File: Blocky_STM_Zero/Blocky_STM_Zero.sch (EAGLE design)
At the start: 37 parts, among them IC3 MCP1703CB, J1 2P-2.0-90D-SMD, U1 MCP73831, U2 STM32L053R8T6, X5 8MHz(16pF)

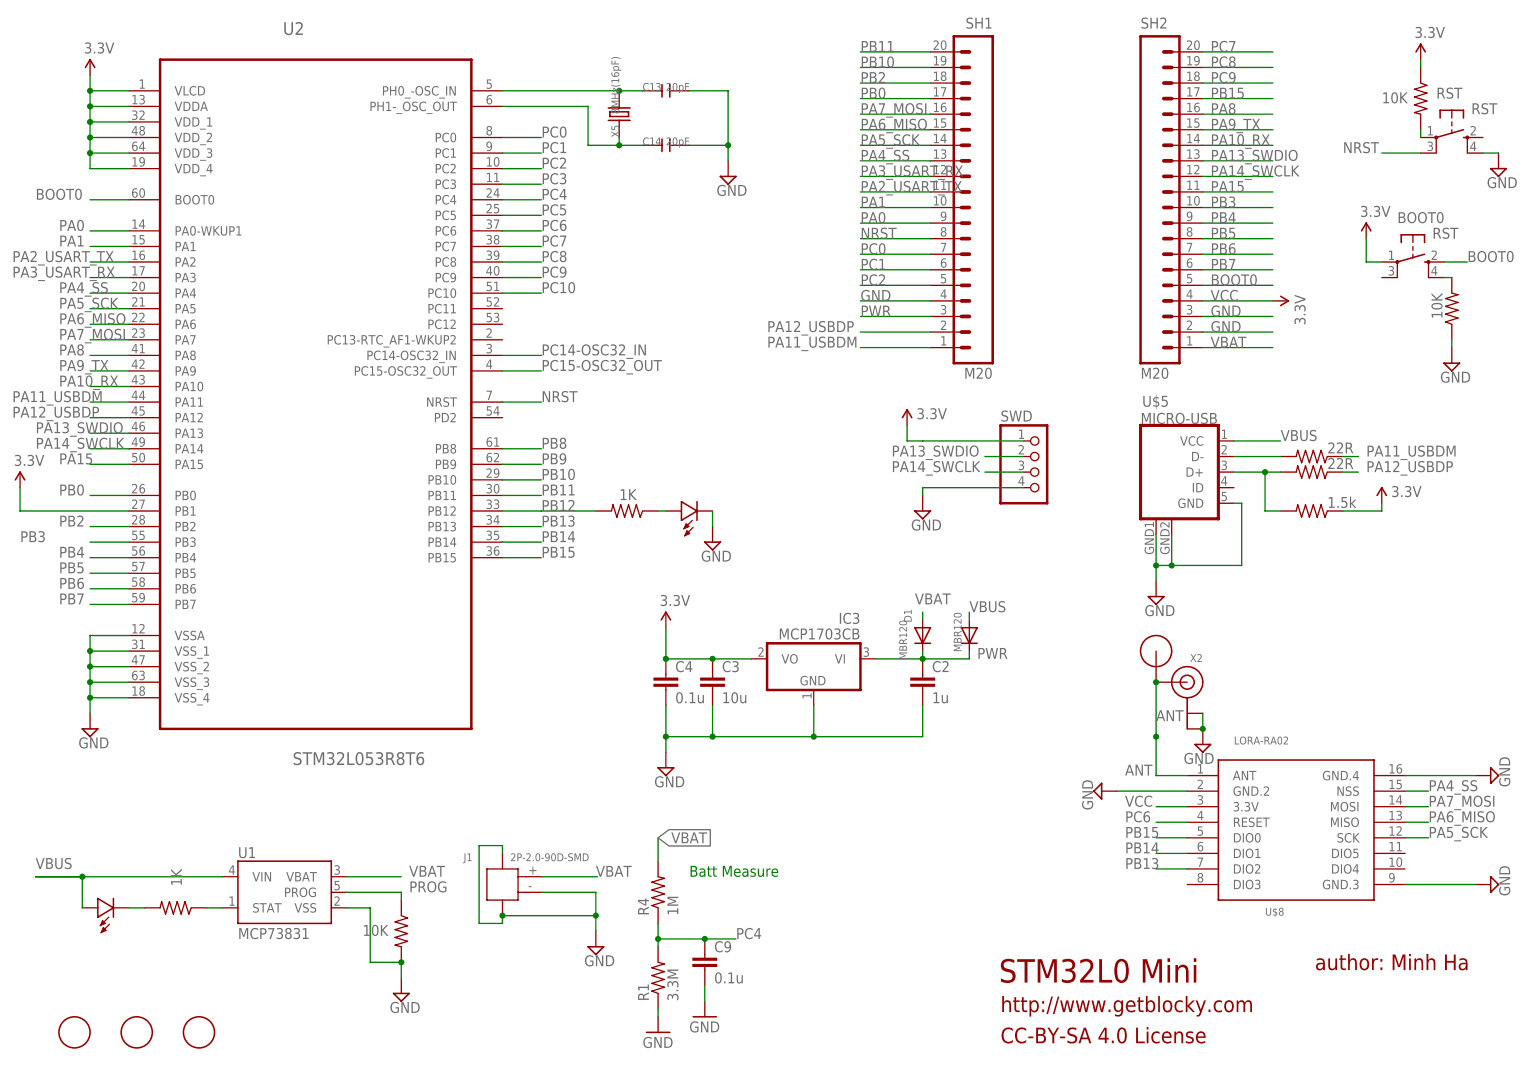
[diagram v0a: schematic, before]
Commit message: Add STM Zero Board
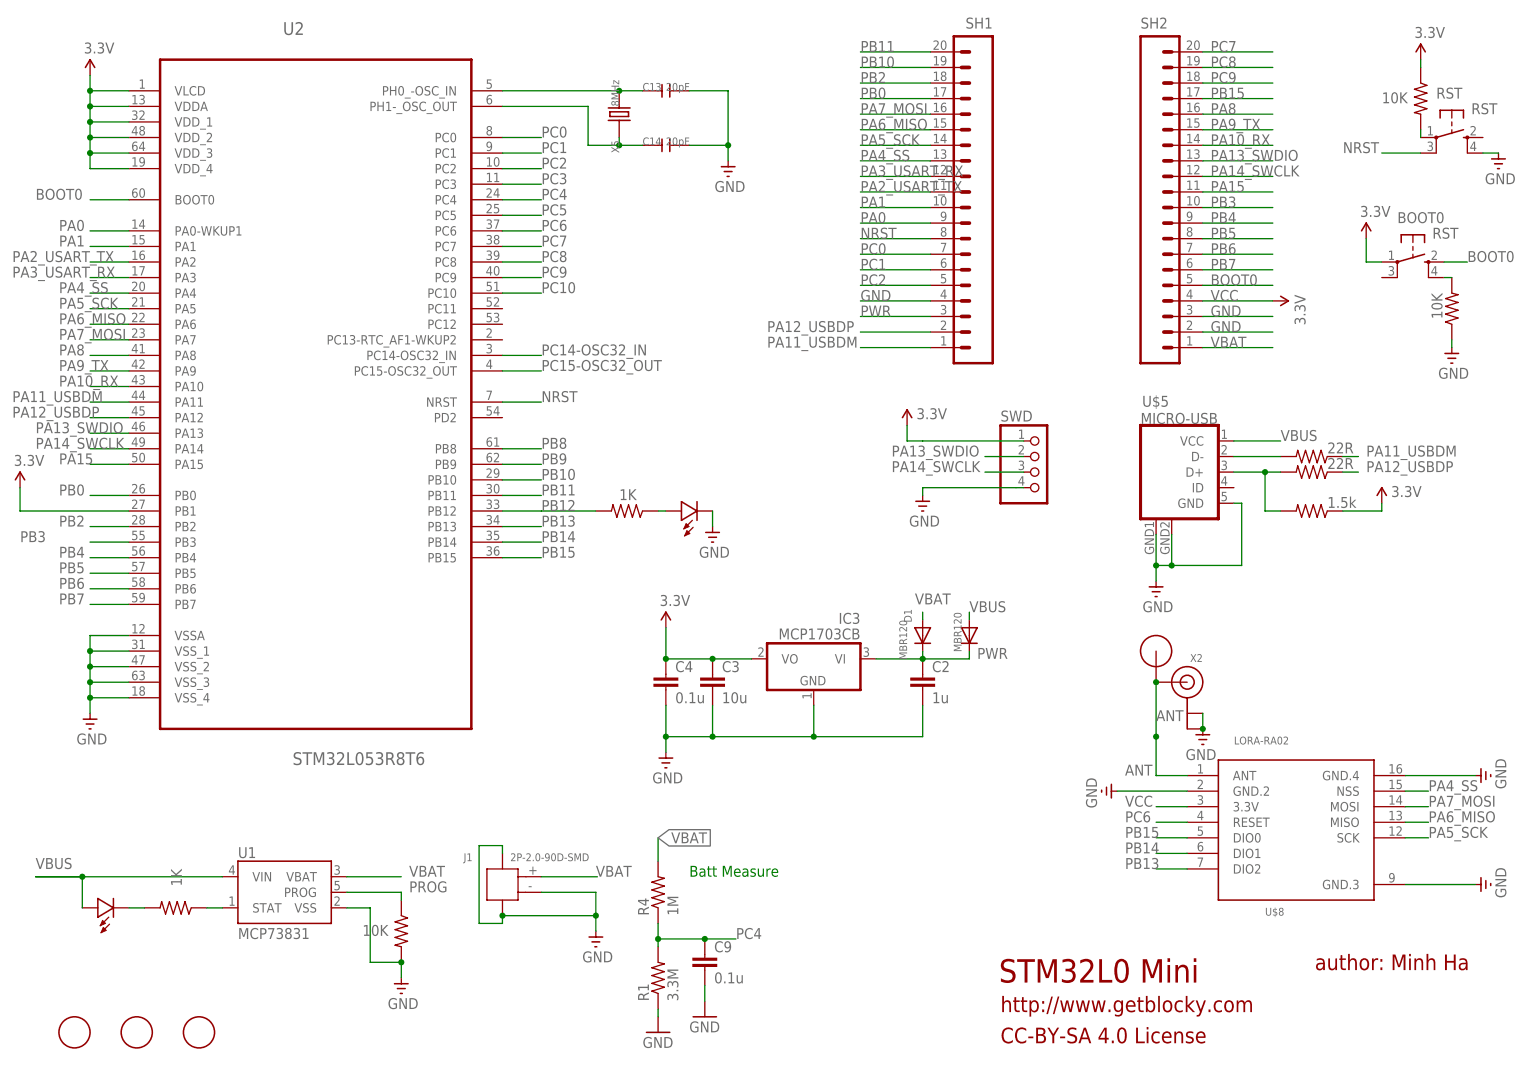
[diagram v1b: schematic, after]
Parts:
- SH1, SH2: value M20 -> (none)
- X5: value 8MHz(16pF) -> 8MHz
- renumbered CHG to CHGR
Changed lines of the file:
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@@
 </classes>
 <parts>
-<part name="FRAME1" library="frames" deviceset="A4L-LOC" device="" value="Moteino"/>
+<part name="FRAME1" library="frames" library_urn="urn:adsk.eagle:library:229" deviceset="A4L-LOC" device="" value="Moteino"/>
 <part name="SUPPLY3" library="SparkFun" deviceset="VCC" device="" value="3.3V"/>
 <part name="SUPPLY10" library="supply2" deviceset="GND" device=""/>
@@
 <part name="U1" library="SparkFun-PowerIC" deviceset="MCP73831" device=""/>
 <part name="R5" library="LowPowerLab" deviceset="RESISTOR" device="0603-RES" value="1K"/>
-<part name="CHG" library="LowPowerLab" deviceset="LED" device="0603" value="RED"/>
+<part name="CHGR" library="LowPowerLab" deviceset="LED" device="0603" value="RED"/>
 <part name="SUPPLY15" library="supply2" deviceset="GND" device=""/>
 <part name="SUPPLY18" library="supply2" deviceset="GND" device=""/>
@@
 <part name="R9" library="LowPowerLab" deviceset="RESISTOR" device="0603-RES" value="10K"/>
 <part name="SUPPLY25" library="supply2" deviceset="GND" device=""/>
-<part name="X5" library="Discrete" deviceset="CRYSTAL*" device="'5032'" value="8MHz(16pF)"/>
+<part name="X5" library="Discrete" deviceset="CRYSTAL*" device="'5032'" value="8MHz"/>
 <part name="C13" library="Discrete" deviceset="C*" device="-0603" value="20pF"/>
 <part name="C14" library="Discrete" deviceset="C*" device="-0603" value="20pF"/>
@@
 <instance part="FRAME1" gate="G$1" x="0" y="0"/>
 <instance part="SUPPLY3" gate="1" x="111.76" y="76.2"/>
-<instance part="SUPPLY10" gate="GND" x="111.76" y="53.34"/>
+<instance part="SUPPLY10" gate="1" x="111.76" y="53.34"/>
 <instance part="IC3" gate="G$1" x="135.89" y="71.12" rot="MR0"/>
 <instance part="C4" gate="G$1" x="111.76" y="66.04"/>
@@
 <instance part="U$1" gate="G$1" x="191.77" y="72.39" rot="R90"/>
 <instance part="U$6" gate="G$1" x="116.84" y="95.25" smashed="yes" rot="R180"/>
-<instance part="SUPPLY6" gate="GND" x="119.38" y="90.17"/>
+<instance part="SUPPLY6" gate="1" x="119.38" y="90.17"/>
 <instance part="SH1" gate="G$1" x="165.1" y="116.84" rot="MR0"/>
 <instance part="SH2" gate="G$1" x="189.23" y="116.84"/>
 <instance part="X2" gate="G$1" x="196.85" y="67.31" rot="MR0"/>
-<instance part="SUPPLY2" gate="GND" x="199.39" y="57.15" rot="MR0"/>
+<instance part="SUPPLY2" gate="1" x="199.39" y="57.15" rot="MR0"/>
 <instance part="U$2" gate="G$1" x="15.24" y="10.16"/>
 <instance part="U$7" gate="G$1" x="25.4" y="10.16"/>
@@
 <attribute name="VALUE" x="30.988" y="36.83" size="1.778" layer="96" rot="R270"/>
 </instance>
-<instance part="CHG" gate="G$1" x="21.59" y="30.48" smashed="yes" rot="R180"/>
-<instance part="SUPPLY15" gate="GND" x="100.33" y="24.13"/>
-<instance part="SUPPLY18" gate="GND" x="68.58" y="16.51"/>
+<instance part="CHGR" gate="G$1" x="21.59" y="30.48" smashed="yes" rot="R180"/>
+<instance part="SUPPLY15" gate="1" x="100.33" y="24.13"/>
+<instance part="SUPPLY18" gate="1" x="68.58" y="16.51"/>
 <instance part="R6" gate="G$1" x="68.58" y="26.67" smashed="yes" rot="R270">
 <attribute name="VALUE" x="62.23" y="25.908" size="1.778" layer="96"/>
@@
 </instance>
 <instance part="U$8" gate="G$1" x="214.63" y="44.45"/>
-<instance part="SUPPLY11" gate="GND" x="182.88" y="49.53" rot="R270"/>
-<instance part="SUPPLY16" gate="GND" x="246.38" y="34.29" rot="R90"/>
-<instance part="SUPPLY20" gate="GND" x="246.38" y="52.07" rot="R90"/>
+<instance part="SUPPLY11" gate="1" x="182.88" y="49.53" rot="R270"/>
+<instance part="SUPPLY16" gate="1" x="246.38" y="34.29" rot="R90"/>
+<instance part="SUPPLY20" gate="1" x="246.38" y="52.07" rot="R90"/>
 <instance part="R4" gate="G$1" x="110.49" y="33.02" rot="R90"/>
 <instance part="R1" gate="G$1" x="110.49" y="19.05" rot="R90"/>
@@
 </instance>
 <instance part="U$5" gate="G$1" x="189.23" y="109.22"/>
-<instance part="SUPPLY21" gate="GND" x="191.77" y="81.28"/>
+<instance part="SUPPLY21" gate="1" x="191.77" y="81.28"/>
 <instance part="U2" gate="A" x="54.61" y="118.11"/>
 <instance part="SUPPLY22" gate="1" x="6.35" y="99.06"/>
@@
 <attribute name="VALUE" x="236.728" y="130.81" size="1.778" layer="96" rot="R270"/>
 </instance>
-<instance part="SUPPLY25" gate="GND" x="240.03" y="119.38"/>
+<instance part="SUPPLY25" gate="1" x="240.03" y="119.38"/>
 <instance part="X5" gate="X" x="104.14" y="160.02" rot="R90"/>
 <instance part="C13" gate="C" x="111.76" y="163.83"/>
 <instance part="C14" gate="C" x="111.76" y="154.94"/>
-<instance part="SUPPLY27" gate="GND" x="121.92" y="149.86"/>
+<instance part="SUPPLY27" gate="1" x="121.92" y="149.86"/>
 <instance part="SUPPLY28" gate="1" x="234.95" y="168.91"/>
 <instance part="R10" gate="G$1" x="234.95" y="162.56" smashed="yes" rot="R270">
 <attribute name="VALUE" x="228.6" y="161.798" size="1.778" layer="96"/>
 </instance>
-<instance part="SUPPLY29" gate="GND" x="247.65" y="151.13"/>
+<instance part="SUPPLY29" gate="1" x="247.65" y="151.13"/>
 <instance part="SUPPLY30" gate="1" x="17.78" y="166.37"/>
 <instance part="RST" gate="G$1" x="240.03" y="156.21" rot="R270"/>
 <instance part="BOOT0" gate="G$1" x="233.68" y="135.89" rot="R270"/>
-<instance part="SUPPLY4" gate="GND" x="17.78" y="59.69"/>
+<instance part="SUPPLY4" gate="1" x="17.78" y="59.69"/>
 <instance part="R3" gate="G$1" x="217.17" y="104.14" smashed="yes" rot="R180">
 <attribute name="VALUE" x="219.71" y="104.648" size="1.778" layer="96"/>
@@
 <attribute name="VALUE" x="152.654" y="110.236" size="1.778" layer="96"/>
 </instance>
-<instance part="SUPPLY9" gate="GND" x="153.67" y="95.25"/>
+<instance part="SUPPLY9" gate="1" x="153.67" y="95.25"/>
 <instance part="SWD" gate="A" x="172.72" y="101.6"/>
 <instance part="U$4" gate="G$1" x="35.56" y="10.16"/>
@@
 <junction x="111.76" y="58.42"/>
 <junction x="135.89" y="58.42"/>
-<pinref part="SUPPLY10" gate="GND" pin="GND"/>
+<pinref part="SUPPLY10" gate="1" pin="GND"/>
 <pinref part="IC3" gate="G$1" pin="GND"/>
 <pinref part="C4" gate="G$1" pin="2"/>
@@
 <segment>
 <pinref part="U$6" gate="G$1" pin="MINUS"/>
-<pinref part="SUPPLY6" gate="GND" pin="GND"/>
+<pinref part="SUPPLY6" gate="1" pin="GND"/>
 <wire x1="119.38" y1="92.71" x2="119.38" y2="95.25" width="0.1524" layer="91"/>
 </segment>
 <segment>
-<pinref part="SUPPLY2" gate="GND" pin="GND"/>
+<pinref part="SUPPLY2" gate="1" pin="GND"/>
 <pinref part="X2" gate="G$1" pin="GND@1"/>
 <pinref part="X2" gate="G$1" pin="GND@0"/>
@@
 <pinref part="J1" gate="G$1" pin="2"/>
 <wire x1="91.44" y1="33.02" x2="100.33" y2="33.02" width="0.1524" layer="91"/>
-<pinref part="SUPPLY15" gate="GND" pin="GND"/>
+<pinref part="SUPPLY15" gate="1" pin="GND"/>
 <wire x1="100.33" y1="26.67" x2="100.33" y2="29.21" width="0.1524" layer="91"/>
 <pinref part="J1" gate="G$1" pin="4"/>
@@
 <wire x1="63.5" y1="21.59" x2="68.58" y2="21.59" width="0.1524" layer="91"/>
 <wire x1="68.58" y1="21.59" x2="68.58" y2="19.05" width="0.1524" layer="91"/>
-<pinref part="SUPPLY18" gate="GND" pin="GND"/>
+<pinref part="SUPPLY18" gate="1" pin="GND"/>
 <pinref part="R6" gate="G$1" pin="2"/>
 <junction x="68.58" y="21.59"/>
@@
 <pinref part="U$8" gate="G$1" pin="GND.2"/>
 <wire x1="196.85" y1="49.53" x2="185.42" y2="49.53" width="0.1524" layer="91"/>
-<pinref part="SUPPLY11" gate="GND" pin="GND"/>
+<pinref part="SUPPLY11" gate="1" pin="GND"/>
 </segment>
 <segment>
 <pinref part="U$8" gate="G$1" pin="GND.3"/>
 <wire x1="232.41" y1="34.29" x2="243.84" y2="34.29" width="0.1524" layer="91"/>
-<pinref part="SUPPLY16" gate="GND" pin="GND"/>
+<pinref part="SUPPLY16" gate="1" pin="GND"/>
 </segment>
 <segment>
 <pinref part="U$8" gate="G$1" pin="GND.4"/>
 <wire x1="232.41" y1="52.07" x2="243.84" y2="52.07" width="0.1524" layer="91"/>
-<pinref part="SUPPLY20" gate="GND" pin="GND"/>
+<pinref part="SUPPLY20" gate="1" pin="GND"/>
 </segment>
 <segment>
@@
 <wire x1="191.77" y1="86.36" x2="191.77" y2="83.82" width="0.1524" layer="91"/>
 <junction x="191.77" y="86.36"/>
-<pinref part="SUPPLY21" gate="GND" pin="GND"/>
+<pinref part="SUPPLY21" gate="1" pin="GND"/>
 </segment>
 <segment>
@@
 <wire x1="115.57" y1="154.94" x2="121.92" y2="154.94" width="0.1524" layer="91"/>
 <junction x="121.92" y="154.94"/>
-<pinref part="SUPPLY27" gate="GND" pin="GND"/>
-</segment>
-<segment>
-<pinref part="SUPPLY29" gate="GND" pin="GND"/>
+<pinref part="SUPPLY27" gate="1" pin="GND"/>
+</segment>
+<segment>
+<pinref part="SUPPLY29" gate="1" pin="GND"/>
 <pinref part="RST" gate="G$1" pin="S1"/>
 <wire x1="245.11" y1="153.67" x2="247.65" y2="153.67" width="0.1524" layer="91"/>
@@
 <junction x="17.78" y="64.77"/>
 <wire x1="17.78" y1="64.77" x2="17.78" y2="62.23" width="0.1524" layer="91"/>
-<pinref part="SUPPLY4" gate="GND" pin="GND"/>
+<pinref part="SUPPLY4" gate="1" pin="GND"/>
 </segment>
 <segment>
@@
 </segment>
 <segment>
-<pinref part="SUPPLY9" gate="GND" pin="GND"/>
+<pinref part="SUPPLY9" gate="1" pin="GND"/>
 <wire x1="153.67" y1="97.79" x2="153.67" y2="99.06" width="0.1524" layer="91"/>
 <wire x1="168.91" y1="99.06" x2="153.67" y2="99.06" width="0.1524" layer="91"/>
@@
 <pinref part="R9" gate="G$1" pin="1"/>
 <wire x1="240.03" y1="123.19" x2="240.03" y2="121.92" width="0.1524" layer="91"/>
-<pinref part="SUPPLY25" gate="GND" pin="GND"/>
+<pinref part="SUPPLY25" gate="1" pin="GND"/>
 </segment>
 <segment>
@@
 <net name="N$9" class="0">
 <segment>
-<pinref part="CHG" gate="G$1" pin="MINUS"/>
+<pinref part="CHGR" gate="G$1" pin="MINUS"/>
 <pinref part="R5" gate="G$1" pin="2"/>
 <wire x1="24.13" y1="30.48" x2="26.67" y2="30.48" width="0.1524" layer="91"/>
@@
 <wire x1="39.37" y1="35.56" x2="16.51" y2="35.56" width="0.1524" layer="91"/>
 <wire x1="16.51" y1="35.56" x2="8.89" y2="35.56" width="0.1524" layer="91"/>
-<pinref part="CHG" gate="G$1" pin="PLUS"/>
+<pinref part="CHGR" gate="G$1" pin="PLUS"/>
 <wire x1="16.51" y1="30.48" x2="16.51" y2="35.56" width="0.1524" layer="91"/>
 <junction x="16.51" y="35.56"/>
